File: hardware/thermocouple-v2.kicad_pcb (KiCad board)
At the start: 2 copper layers, 40 x 30 mm, 35 parts, among them J101 THERM, P1 CON-SENSOR2, P2 DEBUG, P3 BOOT, U1 XMC1100, U102 MAX31856, U103 DRILL, U104 DRILL, U105 DRILL, U106 DRILL

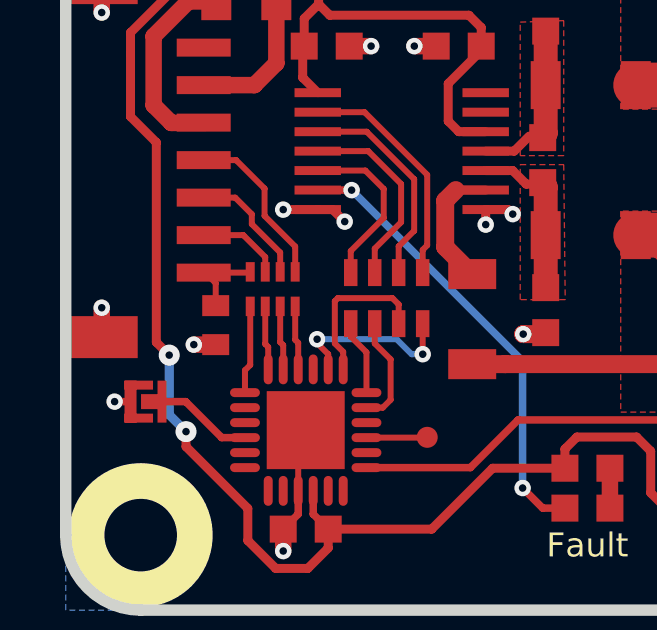
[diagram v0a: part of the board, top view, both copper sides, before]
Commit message: Change capacitor footprint(s) to C0402F
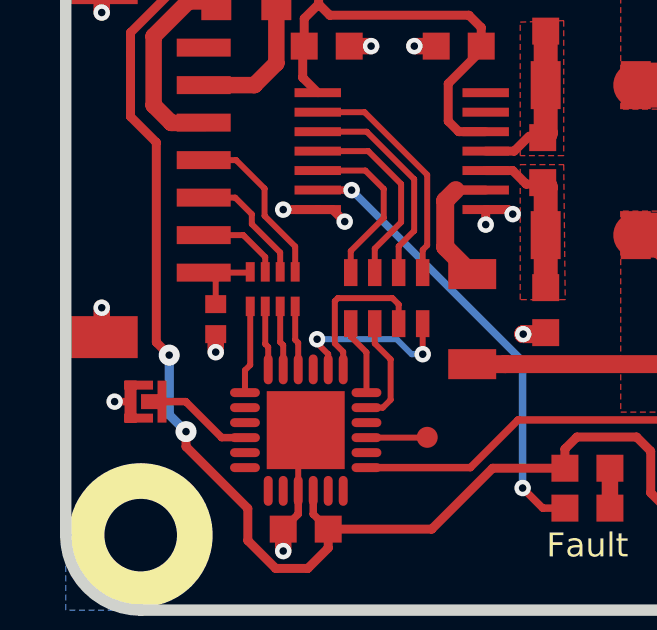
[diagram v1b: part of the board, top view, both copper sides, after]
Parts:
- C1: footprint C0402E -> kicad-libraries:C0402F
- C2: footprint C0805 -> kicad-libraries:C0805
- C3, C4: footprint C0603F -> kicad-libraries:C0603F
- D1: footprint D0603F -> kicad-libraries:D0603F
- P1: footprint CON-SENSOR2 -> kicad-libraries:CON-SENSOR2
- R1: footprint R0603F -> kicad-libraries:R0603F
- RP1: footprint 4X0402 -> kicad-libraries:4X0402
- moved C1 0.20 mm to (155.1, 145.2)
